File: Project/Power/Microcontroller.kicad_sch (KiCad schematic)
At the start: 28 parts, among them J13 I2C, J14 SWD, J15 SPI1, SW1 SW_Push, U14 STM32L422KBTx, U19 INA226, U20 INA226, U21 INA226, U22 INA226

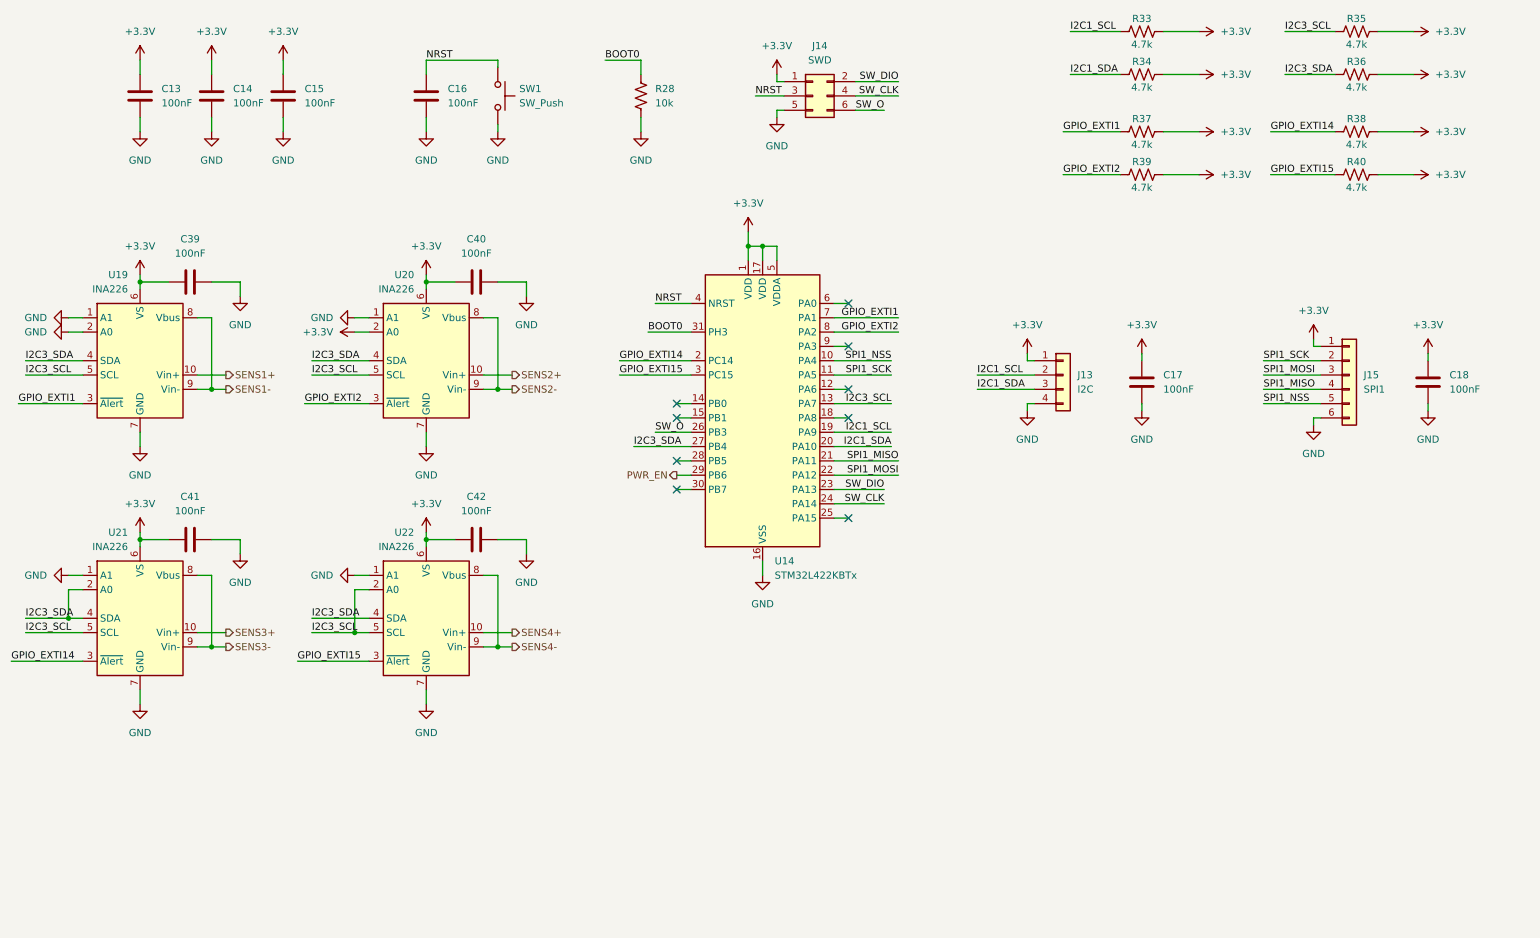
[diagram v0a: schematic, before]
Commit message: Add more sensors for fin module servos
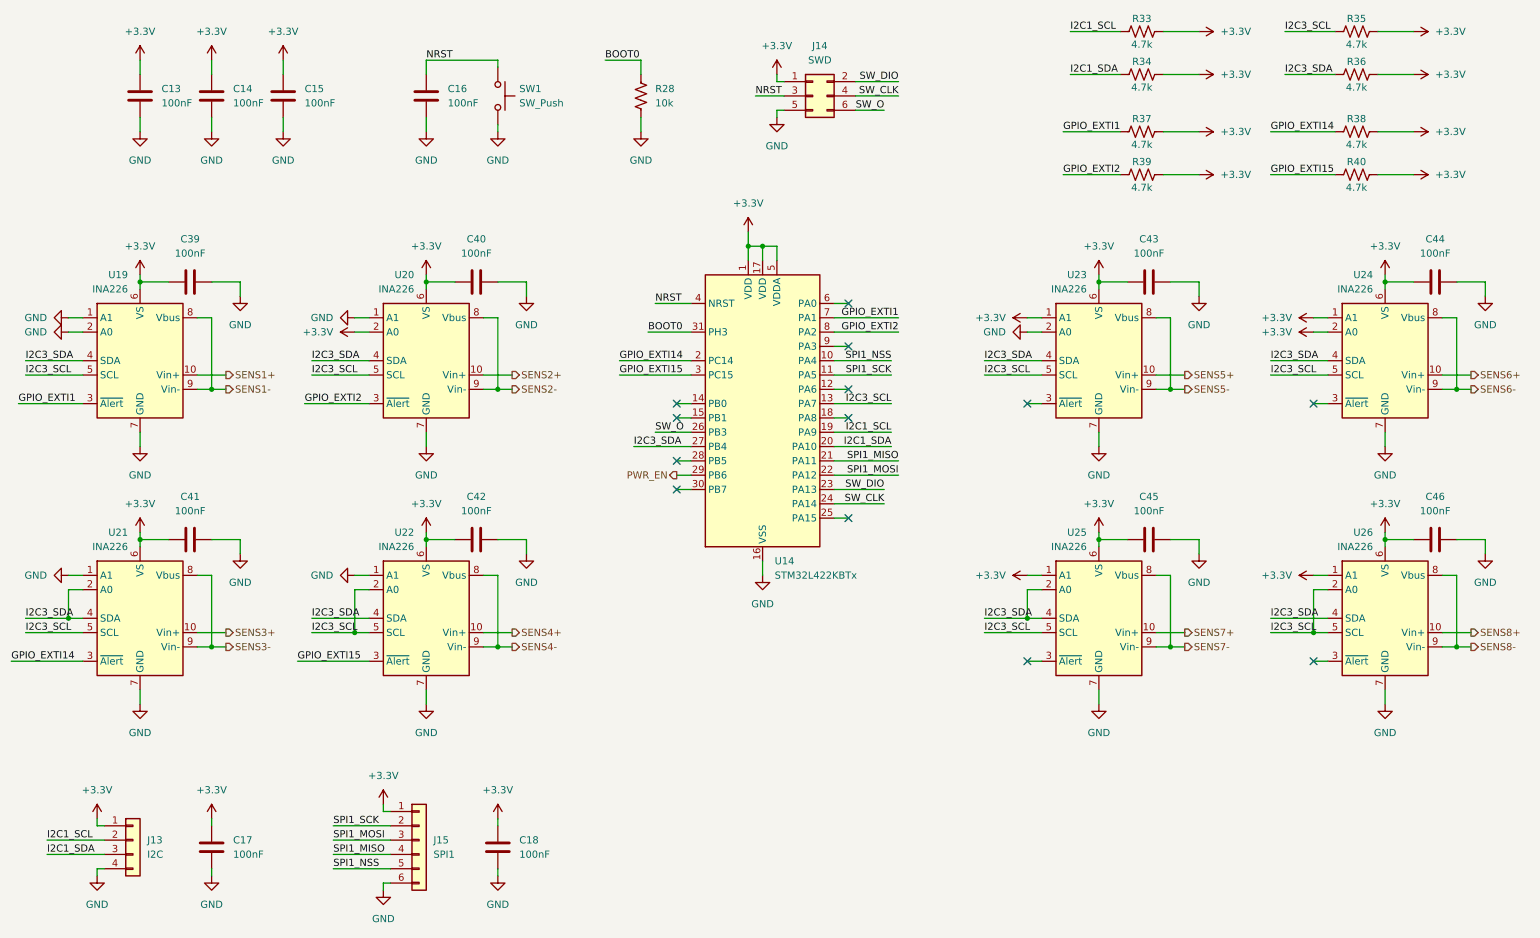
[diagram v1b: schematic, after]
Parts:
- added C43, C44, C45, C46: 100nF, Capacitor_SMD:C_0603_1608Metric, symbol Device:C
- added U23, U24, U25, U26: INA226, Package_SO:VSSOP-10_3x3mm_P0.5mm, symbol Sensor_Energy:INA226
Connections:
- net +3.3V: now also C43.1, C44.1, C45.1, C46.1, U23.1 (A1), U23.6 (VS), U24.1 (A1), U24.2 (A0), U24.6 (VS), U25.1 (A1), U25.6 (VS), U26.1 (A1), U26.6 (VS)
- net GND: now also C43.2, C44.2, C45.2, C46.2, U23.2 (A0), U23.7 (GND), U24.7 (GND), U25.7 (GND), U26.7 (GND)
- net I2C3_SCL: now also U23.5 (SCL), U24.5 (SCL), U25.5 (SCL), U26.2 (A0), U26.5 (SCL)
- net I2C3_SDA: now also U23.4 (SDA), U24.4 (SDA), U25.2 (A0), U25.4 (SDA), U26.4 (SDA)
- new net SENS5+: U23.10 (Vin+)
- new net SENS5-: U23.8 (Vbus), U23.9 (Vin-)
- new net SENS6+: U24.10 (Vin+)
- new net SENS6-: U24.8 (Vbus), U24.9 (Vin-)
- new net SENS7+: U25.10 (Vin+)
- new net SENS7-: U25.8 (Vbus), U25.9 (Vin-)
- new net SENS8+: U26.10 (Vin+)
- new net SENS8-: U26.8 (Vbus), U26.9 (Vin-)
- no-connect marks 9 -> 13
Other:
- moved on the sheet: C17, C18, J13, J15

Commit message: Add LEDs to the microcontroller
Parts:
- added D10: Green, LED_SMD:LED_0603_1608Metric, symbol Device:LED
- added D9: Amber, LED_SMD:LED_0603_1608Metric, symbol Device:LED
- added R45, R46: 330, Resistor_SMD:R_0603_1608Metric, symbol Device:R_US
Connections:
- net GND: now also R45.2, R46.2
- net LED_OUT2: now reaches U14.18 (PA8)
- net LED_OUT2: now also D10.2 (A)
- net LED_OUT1: now reaches U14.9 (PA3)
- net LED_OUT1: now also D9.2 (A)
- new net: D10.1 (K), R46.1
- new net: D9.1 (K), R45.1
- no-connect marks 13 -> 11
